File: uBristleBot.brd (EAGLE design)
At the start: 25.4 x 25.4 mm, 32 parts, among them M1 MOTOR-304-103, M2 MOTOR-304-103, Q1 2N7002BKV, U2 MCP7383X.DFN, U3 LM3668, U4 TPS727XX.DSE

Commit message: Component placement mostly complete. Beginning layout
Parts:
- added C8, C9: .1uF, standardparts:0402
- added U$34: 1X5, headers(2mm):1X5
- moved C3 9.94 mm to (19.7, 1.27), turned to 0 degrees
- moved R7 9.09 mm to (14.0, 6.99), turned to 270 degrees
- moved R1 8.91 mm to (10.2, 9.53), turned to 270 degrees
- moved U4 5.68 mm to (20.3, 7.62), turned to 270 degrees
- moved R8 5.43 mm to (17.1, 6.99), turned to 270 degrees
- moved C4 4.84 mm to (19.7, 5.71), turned to 180 degrees
- moved R3 4.02 mm to (10.2, 6.99), turned to 270 degrees
- moved R6 4.02 mm to (8.26, 9.53), turned to 90 degrees
- moved Q1 3.82 mm to (15.6, 6.99)
- moved R4 3.70 mm to (12.1, 6.99), turned to 270 degrees
- moved R2 3.62 mm to (11.1, 6.99), turned to 270 degrees
- moved R5 3.49 mm to (7.30, 9.53), turned to 270 degrees
- moved C6 3.00 mm to (21.9, 7.62), turned to 270 degrees
- moved L1 1.14 mm to (15.6, 3.17), turned to 180 degrees
- moved C5 0.95 mm to (18.7, 7.62), turned to 90 degrees
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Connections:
- removed net N$7: R1.2, U1.RESET
- new net !RST: R1.2, U$34.2, U1.RESET
- new net P2.1: U$34.3, U1.P2_1
- new net P2.2: U$34.4, U1.P2_2
- net 3.3V: now also U$34.1
- net GND: now also U$34.5
- net N$6: now also C8.2
- net N$8: now also C9.2
- net VMOTOR: now also C8.1, C9.1

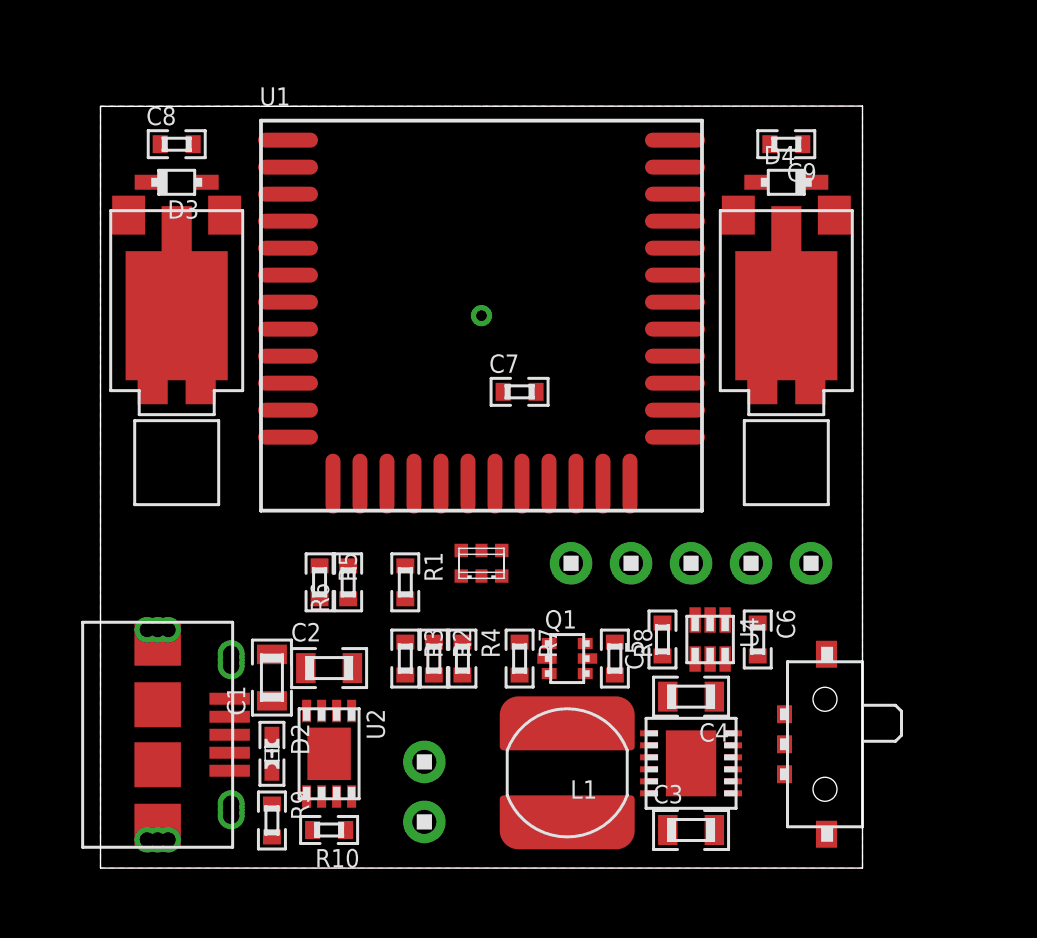
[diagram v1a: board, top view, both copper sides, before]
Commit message: Layout complete and ready for review
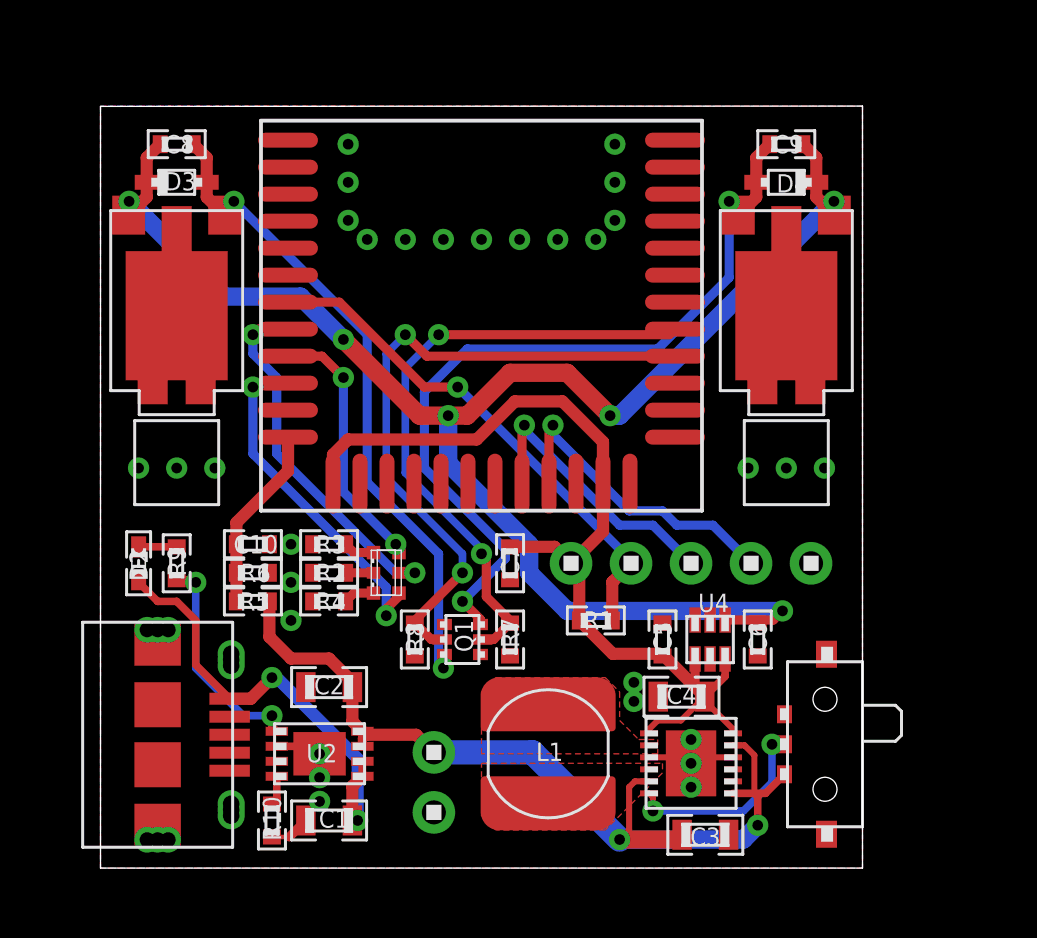
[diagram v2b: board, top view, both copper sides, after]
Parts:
- added C10: .1uF, standardparts:0402
- moved R9 9.14 mm to (2.54, 10.2)
- moved D2 7.75 mm to (1.27, 10.2), turned to 90 degrees
- moved R8 6.70 mm to (10.5, 7.62)
- moved R1 6.48 mm to (16.5, 8.26), turned to 0 degrees
- moved C7 5.72 mm to (13.7, 10.2), turned to 270 degrees
- moved C1 5.13 mm to (7.62, 1.59), turned to 180 degrees
- moved R4 4.84 mm to (7.62, 8.89), turned to 180 degrees
- moved R3 4.58 mm to (7.62, 10.8), turned to 180 degrees
- moved R2 4.51 mm to (7.62, 9.84), turned to 180 degrees
- moved Q1 3.55 mm to (12.1, 7.62), turned to 180 degrees
- moved R6 3.19 mm to (5.08, 9.84), turned to 0 degrees
- moved D1 3.19 mm to (9.53, 9.84), turned to 90 degrees
- moved R5 2.31 mm to (5.08, 8.89), turned to 180 degrees
- moved R10 1.93 mm to (5.71, 1.59), turned to 270 degrees
- moved L1 0.90 mm to (14.9, 3.81)
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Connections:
- net 3.3V: now also U1.AVDD
- net BATT_DIV: now also C10.1
- net GND: now also C10.2, USB2.PAD@1, USB2.PAD@10, USB2.PAD@11, USB2.PAD@12, USB2.PAD@13, USB2.PAD@14, USB2.PAD@15, USB2.PAD@16, USB2.PAD@2, USB2.PAD@3, USB2.PAD@4, USB2.PAD@5, USB2.PAD@6, USB2.PAD@7, USB2.PAD@8, USB2.PAD@9; no longer U1.AVDD
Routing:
- net VMOTOR: track 0.00 -> 55.7 mm, vias 0 -> 6
- net 3.3V: track 0.00 -> 32.2 mm
- net VBAT: track 0.00 -> 32.1 mm, vias 0 -> 2
- net N$8: track 0.00 -> 27.4 mm, vias 0 -> 2
- net N$6: track 0.00 -> 22.9 mm, vias 0 -> 2
- net R_MOTOR: track 0.00 -> 22.0 mm, vias 0 -> 2
- net L_MOTOR: track 0.00 -> 20.6 mm, vias 0 -> 2
- net !RST: track 0.00 -> 17.3 mm, vias 0 -> 1
- net 5.0V: track 0.00 -> 15.6 mm, vias 0 -> 2
- net R_LED: track 0.00 -> 12.3 mm, vias 0 -> 2
- net B_LED: track 0.00 -> 11.6 mm, vias 0 -> 2
- net P2.2: track 0.00 -> 10.7 mm, vias 0 -> 1
- net P2.1: track 0.00 -> 9.54 mm, vias 0 -> 1
- net G_LED: track 0.00 -> 8.74 mm, vias 0 -> 2
- net N$9: track 0.00 -> 7.31 mm, vias 0 -> 2
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- added copper zone on layer 1, net N$12
- added copper zone on layer 1, net N$5
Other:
- board text added: "!RST"
- board text added: "3.3v"
- board text added: "Cruz Monrreal II"
- board text added: "GND"
- board text added: "P2.1"
- board text added: "P2.2"
- board text added: "VBAT"
- board text added: "uBristleBot"

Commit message: Updated Inuctor and LED layer parts, and moved PWM pins. Ripped up programming connector in prep for Pogo Pins
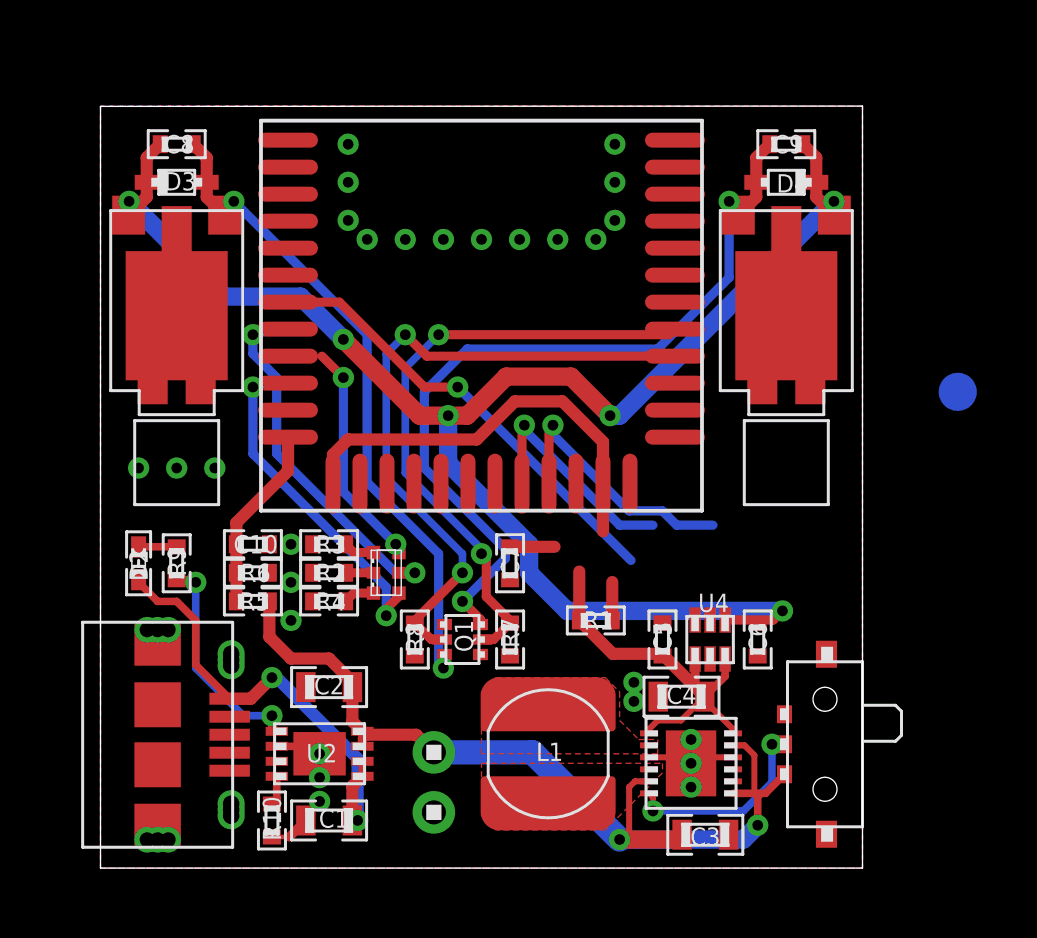
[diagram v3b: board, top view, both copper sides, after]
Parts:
- removed U$34: 1X5, headers(2mm):1X5
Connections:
- net !RST: no longer U$34.2
- net 3.3V: no longer U$34.1
- net B_LED: now also U1.P0_6; no longer U1.P0_5
- net GND: no longer U$34.5
- net G_LED: now also U1.P0_5; no longer U1.P0_4
- net P2.1: no longer U$34.3
- net P2.2: no longer U$34.4
- net R_LED: now also U1.P0_4; no longer U1.P0_3
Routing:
- net 3.3V: track 32.2 -> 29.6 mm
- net P2.1: track 9.54 -> 7.74 mm
- net P2.2: track 10.7 -> 8.90 mm
- net G_LED: track 8.74 -> 7.61 mm
- net B_LED: track 11.6 -> 10.6 mm
- net R_LED: track 12.3 -> 11.3 mm
- net !RST: track 17.3 -> 16.3 mm
- net GND: vias 30 -> 27
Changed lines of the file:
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@@
 <setting verticaltext="up"/>
 </settings>
-<grid distance="25" unitdist="mil" unit="mil" style="dots" multiple="2" display="yes" altdistance="12.5" altunitdist="mil" altunit="mil"/>
+<grid distance="25" unitdist="mil" unit="mil" style="dots" multiple="2" display="yes" altdistance="5" altunitdist="mil" altunit="mil"/>
 <layers>
 <layer number="1" name="Top" color="4" fill="1" visible="yes" active="yes"/>
@@
 <text x="24.765" y="18.7325" size="1.778" layer="52" font="vector" ratio="12" rot="MR0">uBristleBot</text>
 <text x="24.765" y="17.4625" size="1.016" layer="52" font="vector" ratio="12" rot="MR0">Cruz Monrreal II</text>
+<circle x="28.575" y="15.875" radius="0.3175" width="0.635" layer="16"/>
 </plain>
 <attributes>
@@
 <attribute name="NAME" x="22.9235" y="24.13" size="0.6096" layer="25" font="vector" ratio="12" rot="R180" align="center"/>
 </element>
-<element name="U$34" library="headers(2mm)" package="1X5" value="1X5" x="19.685" y="10.16" smashed="yes"/>
 <element name="C10" library="standardparts" package="0402" value=".1uF" x="5.08" y="10.795" smashed="yes">
 <attribute name="NAME" x="5.17525" y="10.795" size="0.6096" layer="25" font="vector" ratio="12" align="center"/>
@@
 <contactref element="C7" pad="2"/>
 <contactref element="U$31" pad="2"/>
-<contactref element="U$34" pad="5"/>
 <wire x1="21.085" y1="3.6925" x2="19.885" y2="3.6925" width="0.2032" layer="1"/>
 <wire x1="19.885" y1="3.6925" x2="19.685" y2="3.4925" width="0.2032" layer="1"/>
@@
 <via x="3.81" y="13.335" extent="1-16" drill="0.3556"/>
 <via x="1.27" y="13.335" extent="1-16" drill="0.3556"/>
-<via x="21.59" y="13.335" extent="1-16" drill="0.3556"/>
-<via x="22.86" y="13.335" extent="1-16" drill="0.3556"/>
-<via x="24.13" y="13.335" extent="1-16" drill="0.3556"/>
 </signal>
 <signal name="5.0V">
@@
 <signal name="R_LED">
 <contactref element="D1" pad="2"/>
-<contactref element="U1" pad="P0_3"/>
 <wire x1="5.87375" y1="13.81125" x2="5.87375" y2="16.35125" width="0.3048" layer="16"/>
 <wire x1="5.87375" y1="16.35125" x2="5.08" y2="17.145" width="0.3048" layer="16"/>
@@
 <via x="5.08" y="17.78" extent="1-16" drill="0.3556"/>
 <wire x1="5.08" y1="17.78" x2="5.265" y2="17.965" width="0.3048" layer="1"/>
-<wire x1="5.265" y1="17.965" x2="6.25" y2="17.965" width="0.3048" layer="1"/>
 <wire x1="9.95" y1="9.8425" x2="10.4775" y2="9.8425" width="0.3048" layer="1"/>
 <via x="10.4775" y="9.8425" extent="1-16" drill="0.3556"/>
 <wire x1="10.4775" y1="9.8425" x2="9.8425" y2="9.8425" width="0.3048" layer="16"/>
 <wire x1="9.8425" y1="9.8425" x2="5.87375" y2="13.81125" width="0.3048" layer="16"/>
+<contactref element="U1" pad="P0_4"/>
+<wire x1="5.87375" y1="16.35125" x2="6.25" y2="17.065" width="0" layer="19" extent="1-16"/>
 </signal>
 <signal name="G_LED">
 <contactref element="D1" pad="3"/>
-<contactref element="U1" pad="P0_4"/>
 <wire x1="8.09625" y1="12.54125" x2="8.09625" y2="16.35125" width="0.3048" layer="16"/>
 <via x="8.09625" y="16.35125" extent="1-16" drill="0.3556"/>
 <wire x1="8.09625" y1="16.35125" x2="7.3825" y2="17.065" width="0.3048" layer="1"/>
-<wire x1="7.3825" y1="17.065" x2="6.25" y2="17.065" width="0.3048" layer="1"/>
 <wire x1="9.95" y1="10.5175" x2="9.95" y2="10.6875" width="0.3048" layer="1"/>
 <wire x1="9.95" y1="10.6875" x2="9.8425" y2="10.795" width="0.3048" layer="1"/>
 <via x="9.8425" y="10.795" extent="1-16" drill="0.3556"/>
 <wire x1="9.8425" y1="10.795" x2="8.09625" y2="12.54125" width="0.3048" layer="16"/>
+<contactref element="U1" pad="P0_5"/>
+<wire x1="7.3825" y1="17.065" x2="6.25" y2="16.165" width="0" layer="19" extent="1-1"/>
 </signal>
 <signal name="B_LED">
 <contactref element="D1" pad="1"/>
-<contactref element="U1" pad="P0_5"/>
 <via x="5.08" y="16.03375" extent="1-16" drill="0.3556"/>
 <wire x1="5.08" y1="16.03375" x2="5.21125" y2="16.165" width="0.3048" layer="1"/>
-<wire x1="5.21125" y1="16.165" x2="6.25" y2="16.165" width="0.3048" layer="1"/>
 <wire x1="5.08" y1="13.81125" x2="5.08" y2="16.03375" width="0.3048" layer="16"/>
 <via x="9.525" y="8.41375" extent="1-16" drill="0.3556"/>
@@
 <wire x1="9.525" y1="8.636" x2="9.95" y2="9.061" width="0.3048" layer="1"/>
 <wire x1="9.95" y1="9.061" x2="9.95" y2="9.1675" width="0.3048" layer="1"/>
+<contactref element="U1" pad="P0_6"/>
+<wire x1="5.21125" y1="16.165" x2="6.25" y2="15.265" width="0" layer="19" extent="1-1"/>
 </signal>
 <signal name="3.3V">
@@
 <contactref element="U4" pad="4"/>
 <contactref element="C7" pad="1"/>
-<contactref element="U$34" pad="1"/>
 <wire x1="20.82" y1="6.97" x2="20.82" y2="6.3925" width="0.254" layer="1"/>
 <wire x1="20.82" y1="6.3925" x2="20.1425" y2="5.715" width="0.254" layer="1"/>
@@
 <wire x1="20.1425" y1="5.575" x2="20.1425" y2="5.715" width="0.2032" layer="1"/>
 <wire x1="16.75" y1="12.815" x2="16.75" y2="11.225" width="0.4064" layer="1"/>
-<wire x1="16.75" y1="11.225" x2="15.685" y2="10.16" width="0.4064" layer="1"/>
 <wire x1="18.7325" y1="7.07" x2="18.7875" y2="7.07" width="0.4064" layer="1"/>
 <wire x1="18.7875" y1="7.07" x2="20.1425" y2="5.715" width="0.4064" layer="1"/>
@@
 <wire x1="18.65875" y1="7.14375" x2="17.07125" y2="7.14375" width="0.4064" layer="1"/>
 <wire x1="17.07125" y1="7.14375" x2="15.96" y2="8.255" width="0.4064" layer="1"/>
-<wire x1="15.685" y1="10.16" x2="15.96" y2="9.885" width="0.4064" layer="1"/>
 <wire x1="15.96" y1="9.885" x2="15.96" y2="8.255" width="0.4064" layer="1"/>
 <contactref element="U1" pad="AVDD"/>
@@
 <wire x1="16.75" y1="14.20625" x2="16.75" y2="12.815" width="0.4064" layer="1"/>
 <wire x1="13.6525" y1="10.71" x2="15.135" y2="10.71" width="0.4064" layer="1"/>
-<wire x1="15.135" y1="10.71" x2="15.685" y2="10.16" width="0.4064" layer="1"/>
+<wire x1="15.96" y1="9.885" x2="15.135" y2="10.71" width="0" layer="19" extent="1-1"/>
+<wire x1="16.75" y1="11.225" x2="15.96" y2="9.885" width="0" layer="19" extent="1-1"/>
 </signal>
 <signal name="N$2">
@@
 <contactref element="R1" pad="2"/>
 <contactref element="U1" pad="RESET"/>
-<contactref element="U$34" pad="2"/>
 <wire x1="17.06" y1="8.255" x2="17.06" y2="9.535" width="0.4064" layer="1"/>
-<wire x1="17.06" y1="9.535" x2="17.685" y2="10.16" width="0.4064" layer="1"/>
-<wire x1="17.685" y1="10.16" x2="17.685" y2="10.255" width="0.3048" layer="16"/>
 <wire x1="17.685" y1="10.255" x2="11.90625" y2="16.03375" width="0.3048" layer="16"/>
 <via x="11.90625" y="16.03375" extent="1-16" drill="0.3556"/>
@@
 <wire x1="10.795" y1="16.03375" x2="7.96375" y2="18.865" width="0.3048" layer="1"/>
 <wire x1="7.96375" y1="18.865" x2="6.25" y2="18.865" width="0.3048" layer="1"/>
+<wire x1="17.685" y1="10.255" x2="17.06" y2="9.535" width="0" layer="19" extent="1-16"/>
 </signal>
 <signal name="BATT_DIV">
@@
 <via x="11.58875" y="15.08125" extent="1-16" drill="0.3556"/>
 <wire x1="11.58875" y1="15.08125" x2="12.22375" y2="15.08125" width="0.6096" layer="1"/>
-<wire x1="12.22375" y1="15.08125" x2="13.6525" y2="16.51" width="0.6096" layer="1"/>
-<wire x1="13.6525" y1="16.51" x2="15.5575" y2="16.51" width="0.6096" layer="1"/>
-<wire x1="15.5575" y1="16.51" x2="16.98625" y2="15.08125" width="0.6096" layer="1"/>
+<wire x1="12.22375" y1="15.08125" x2="13.5255" y2="16.383" width="0.6096" layer="1"/>
+<wire x1="13.5255" y1="16.383" x2="15.6845" y2="16.383" width="0.6096" layer="1"/>
+<wire x1="15.6845" y1="16.383" x2="16.98625" y2="15.08125" width="0.6096" layer="1"/>
 <via x="16.98625" y="15.08125" extent="1-16" drill="0.3556"/>
 <wire x1="16.98625" y1="15.08125" x2="17.30375" y2="15.08125" width="0.6096" layer="16"/>
@@
 <signal name="P2.1">
 <contactref element="U1" pad="P2_1"/>
-<contactref element="U$34" pad="3"/>
-<wire x1="19.685" y1="10.16" x2="18.415" y2="11.43" width="0.3048" layer="16"/>
 <wire x1="18.415" y1="11.43" x2="17.30375" y2="11.43" width="0.3048" layer="16"/>
 <wire x1="17.30375" y1="11.43" x2="14.12875" y2="14.605" width="0.3048" layer="16"/>
@@
 <signal name="P2.2">
 <contactref element="U1" pad="P2_2"/>
-<contactref element="U$34" pad="4"/>
-<wire x1="21.685" y1="10.16" x2="20.415" y2="11.43" width="0.3048" layer="16"/>
 <wire x1="20.415" y1="11.43" x2="19.20875" y2="11.43" width="0.3048" layer="16"/>
 <wire x1="19.20875" y1="11.43" x2="18.7325" y2="11.90625" width="0.3048" layer="16"/>

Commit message: Finished layout of v0.2
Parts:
- added TP1, TP2, TP3, TP4, TP5: PCB_PAD.42MIL, mil_max:0906-0_PAD
- added U$34: 1X1, headers.edge(.1in):1X1
- U$31: value 1X2 -> 1X1; device headers(2mm):1X2 -> headers.edge(.1in):1X1
- moved SW1 25.4 mm to (0.00, 4.13), turned to 270 degrees
- moved D2 22.2 mm to (23.5, 9.53), turned to 0 degrees
- moved R9 21.0 mm to (23.5, 10.8), turned to 180 degrees
- moved USB2 21.0 mm to (22.9, 4.45), turned to 90 degrees
- moved C3 15.5 mm to (5.40, 5.87), turned to 180 degrees
- moved C4 14.7 mm to (5.40, 1.11), turned to 0 degrees
- moved U3 14.3 mm to (5.40, 3.49), turned to 90 degrees
- moved C6 12.1 mm to (10.2, 10.5), turned to 0 degrees
- moved C2 11.1 mm to (18.1, 9.84)
- moved C1 11.1 mm to (17.8, 6.03)
- moved U2 11.0 mm to (17.5, 7.94)
- moved R10 10.6 mm to (14.9, 6.83), turned to 90 degrees
- moved U4 10.2 mm to (10.2, 8.89), turned to 0 degrees
- moved R1 9.29 mm to (7.30, 9.53)
- moved C5 8.58 mm to (10.2, 7.30), turned to 180 degrees
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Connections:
- net !RST: now also TP2.PAD
- net 3.3V: now also TP1.PAD
- net GND: now also SW1.1, TP5.PAD, U$34.1; no longer SW1.2, U$31.2
- net P2.1: now also TP3.PAD
- net P2.2: now also TP4.PAD
- net VBAT: now also SW1.2; no longer SW1.1
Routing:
- net 3.3V: track 29.6 -> 50.4 mm, vias 0 -> 4
- net VMOTOR: track 55.6 -> 45.6 mm, vias 6 -> 5
- net VBAT: track 32.1 -> 42.1 mm, vias 2 -> 4
- net R_MOTOR: track 22.0 -> 13.8 mm
- net P2.2: track 8.90 -> 1.40 mm
- net P2.1: track 7.74 -> 2.41 mm
- net 5.0V: track 15.6 -> 10.7 mm, vias 2 -> 0
- net B_LED: track 10.6 -> 5.97 mm, vias 2 -> 0
- net L_MOTOR: track 20.6 -> 16.9 mm, vias 2 -> 0
- net N$8: track 27.4 -> 23.9 mm
- net !RST: track 16.3 -> 12.9 mm, vias 1 -> 2
- net R_LED: track 11.3 -> 7.99 mm
- net 3.3V_EN: track 6.69 -> 5.29 mm
- net GND: track 5.85 -> 4.49 mm, vias 27 -> 28
- net N$9: track 7.31 -> 7.99 mm
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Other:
- board text added: "TheNextPlateau.com"
- board text added: "v0.2"
- board text removed: "!RST"
- board text removed: "3.3v"
- board text removed: "P2.1"
- board text removed: "P2.2"
